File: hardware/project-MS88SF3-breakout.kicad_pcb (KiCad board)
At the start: 4 copper layers, 22.9 x 50.8 mm, 28 parts, among them J1 Conn_02x05_Odd_Even, J2 S2B-PH-SM4-TB(LF)(SN), J3 USB4105-GF-A, J4 Conn_01x12_Male, J5 Conn_01x16_Male, U1 MS88SF3_NRF52840

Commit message: Update pcb from schematic
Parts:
- removed Ref**: Val**, drawing:bear-body_silk_16x16
- removed S1: 435151014824, 435151014824:435151014824
- added SW1: PTS810_SJM_250_SMTR_LFS, PTS810-SJM-250-SMTR-LFS:SW_PTS810_SJM_250_SMTR_LFS, F.Cu at (25.3, 118.0)
- J4: value Conn_01x12_Male -> Conn_01x12_Pin; moved to F.Cu
- J5: value Conn_01x16_Male -> Conn_01x16_Pin; moved to F.Cu
- JP1: footprint Jumper:SolderJumper-2_P1.3mm_Bridged_RoundedPad1.0x1.5mm -> mine:SolderJumper-2_P1.3mm_Bridged_RoundedPad1.0x1.5mm
- JP2: footprint Jumper:SolderJumper-2_P1.3mm_Open_RoundedPad1.0x1.5mm -> mine:SolderJumper-2_P1.3mm_Open_RoundedPad1.0x1.5mm
- moved J5 38.6 mm to (19.1, 85.4), turned to 0 degrees
- moved J4 13.7 mm to (23.8, 85.4), turned to 0 degrees
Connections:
- J1 pad 7: Net-(J1-Pad7) -> unconnected-(J1-Pin_7-Pad7)
- J3 pad A8: Net-(J3-PadA8) -> unconnected-(J3-SBU1-PadA8)
- J3 pad B8: Net-(J3-PadB8) -> unconnected-(J3-SBU2-PadB8)
- J4 pad 11: Net-(J4-Pad11) -> unconnected-(J4-Pin_11-Pad11)
- J5 pad 4: /RX -> /P0.24
- J5 pad 6: /TX -> /P0.20
- U1 pad 11: Net-(U1-Pad11) -> unconnected-(U1-P0.28/AIN4-Pad11)
- U1 pad 12: Net-(U1-Pad12) -> unconnected-(U1-P0.30/AIN6-Pad12)
- U1 pad 13: Net-(U1-Pad13) -> unconnected-(U1-P0.31/AIN7-Pad13)
- U1 pad 14: Net-(U1-Pad14) -> unconnected-(U1-P0.27-Pad14)
- U1 pad 17: Net-(U1-Pad17) -> unconnected-(U1-P0.26-Pad17)
- U1 pad 19: Net-(U1-Pad19) -> /RX
- U1 pad 2: Net-(U1-Pad2) -> unconnected-(U1-P1.11-Pad2)
- U1 pad 20: Net-(U1-Pad20) -> /TX
- U1 pad 21: Net-(U1-Pad21) -> unconnected-(U1-P1.08-Pad21)
- U1 pad 22: Net-(U1-Pad22) -> unconnected-(U1-P0.11/TRACEDATA2-Pad22)
- U1 pad 23: Net-(U1-Pad23) -> unconnected-(U1-P0.00/XL1-Pad23)
- U1 pad 24: Net-(U1-Pad24) -> unconnected-(U1-P0.01/XL2-Pad24)
- U1 pad 25: Net-(U1-Pad25) -> unconnected-(U1-P0.08-Pad25)
- U1 pad 26: Net-(U1-Pad26) -> unconnected-(U1-P1.09/TRACEDATA3-Pad26)
- U1 pad 27: Net-(U1-Pad27) -> unconnected-(U1-P0.12/TRACEDATA1-Pad27)
- U1 pad 29: Net-(U1-Pad29) -> unconnected-(U1-P0.16-Pad29)
- U1 pad 3: Net-(U1-Pad3) -> unconnected-(U1-P1.12-Pad3)
- U1 pad 30: Net-(U1-Pad30) -> unconnected-(U1-P0.14-Pad30)
- U1 pad 44: /TX -> /P0.20
- U1 pad 46: /RX -> /P0.24
- U1 pad 47: Net-(U1-Pad47) -> unconnected-(U1-P1.00/TRACEDATA0-Pad47)
- U1 pad 51: Net-(U1-Pad51) -> unconnected-(U1-RF-Pad51)
- U1 pad 52: Net-(U1-Pad52) -> unconnected-(U1-P1.02-Pad52)
- U1 pad 53: Net-(U1-Pad53) -> unconnected-(U1-P1.04-Pad53)
- U1 pad 54: Net-(U1-Pad54) -> unconnected-(U1-P1.06-Pad54)
- U1 pad 57: Net-(U1-Pad57) -> unconnected-(U1-P1.07-Pad57)
- U1 pad 58: Net-(U1-Pad58) -> unconnected-(U1-P1.05-Pad58)
- U1 pad 59: Net-(U1-Pad59) -> unconnected-(U1-P1.01-Pad59)
- U1 pad 60: Net-(U1-Pad60) -> unconnected-(U1-P1.03-Pad60)
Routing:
- net /P0.20: track 0.00 -> 15.2 mm
- net /TX: track 34.6 -> 19.4 mm
- net /P0.24: track 0.00 -> 11.4 mm
- net /RX: track 37.1 -> 25.7 mm

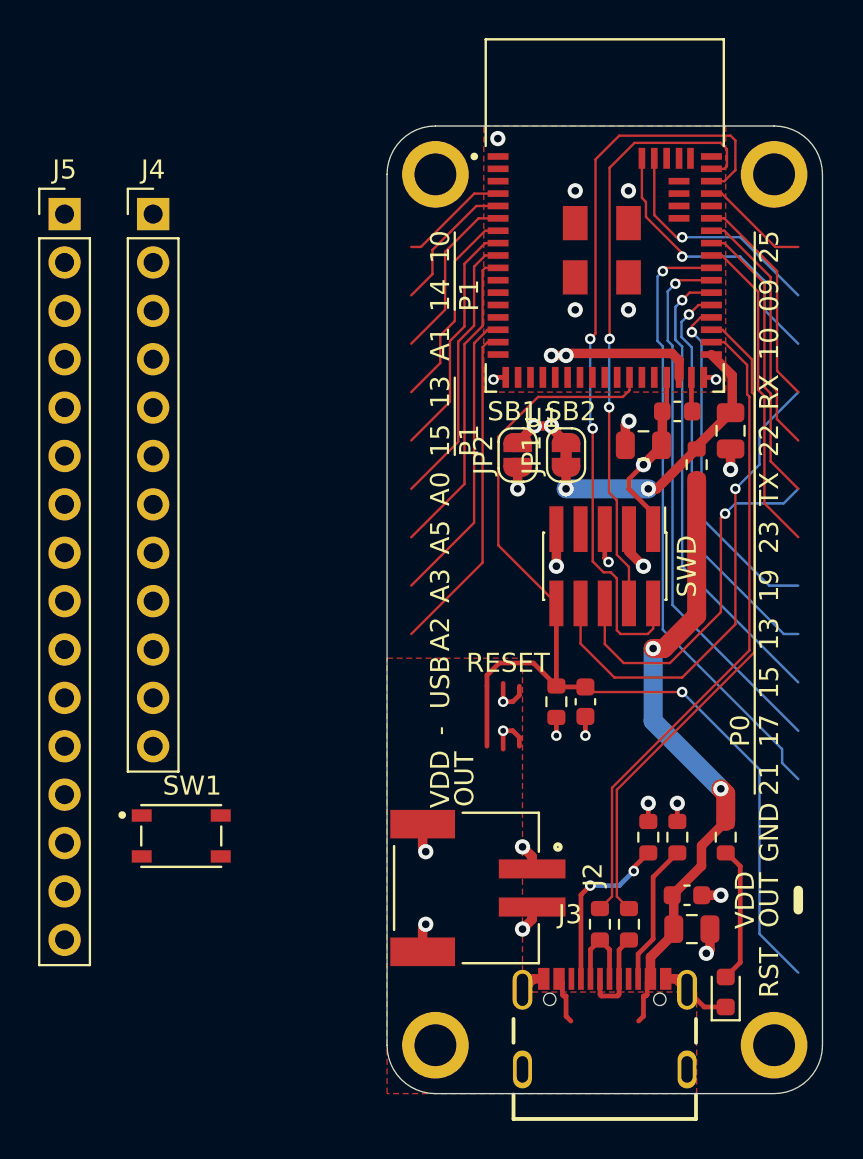
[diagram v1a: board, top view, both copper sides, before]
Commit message: Remove unused traces
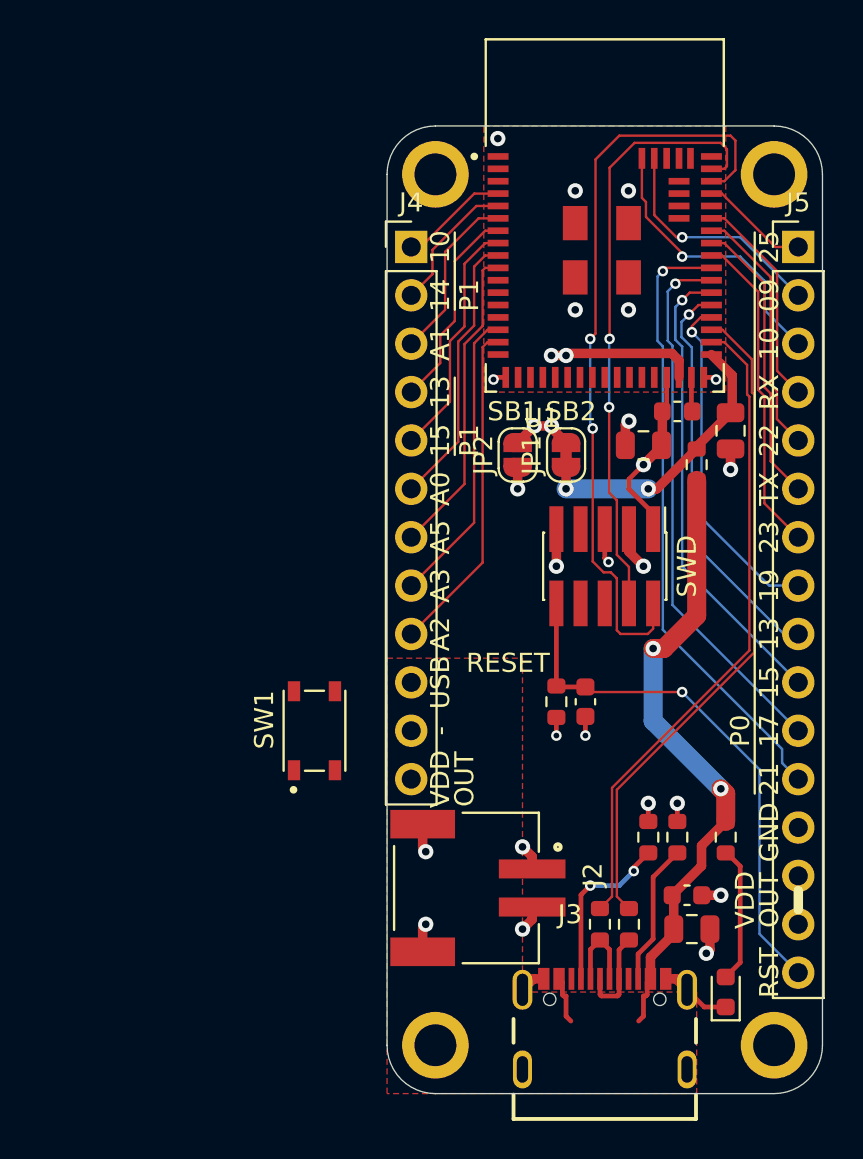
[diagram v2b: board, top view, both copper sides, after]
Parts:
- moved J5 38.6 mm to (57.7, 87.1)
- moved J4 13.7 mm to (37.3, 87.1)
- moved SW1 8.91 mm to (32.3, 112.5), turned to 90 degrees
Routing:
- net /RESET: track 55.1 -> 28.3 mm
- net /RX: track 25.7 -> 0.00 mm, vias 1 -> 0
- net /TX: track 19.4 -> 0.00 mm, vias 1 -> 0
- net GND: track 29.5 -> 24.6 mm, vias 22 -> 20

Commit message: Update pin headers from schematic
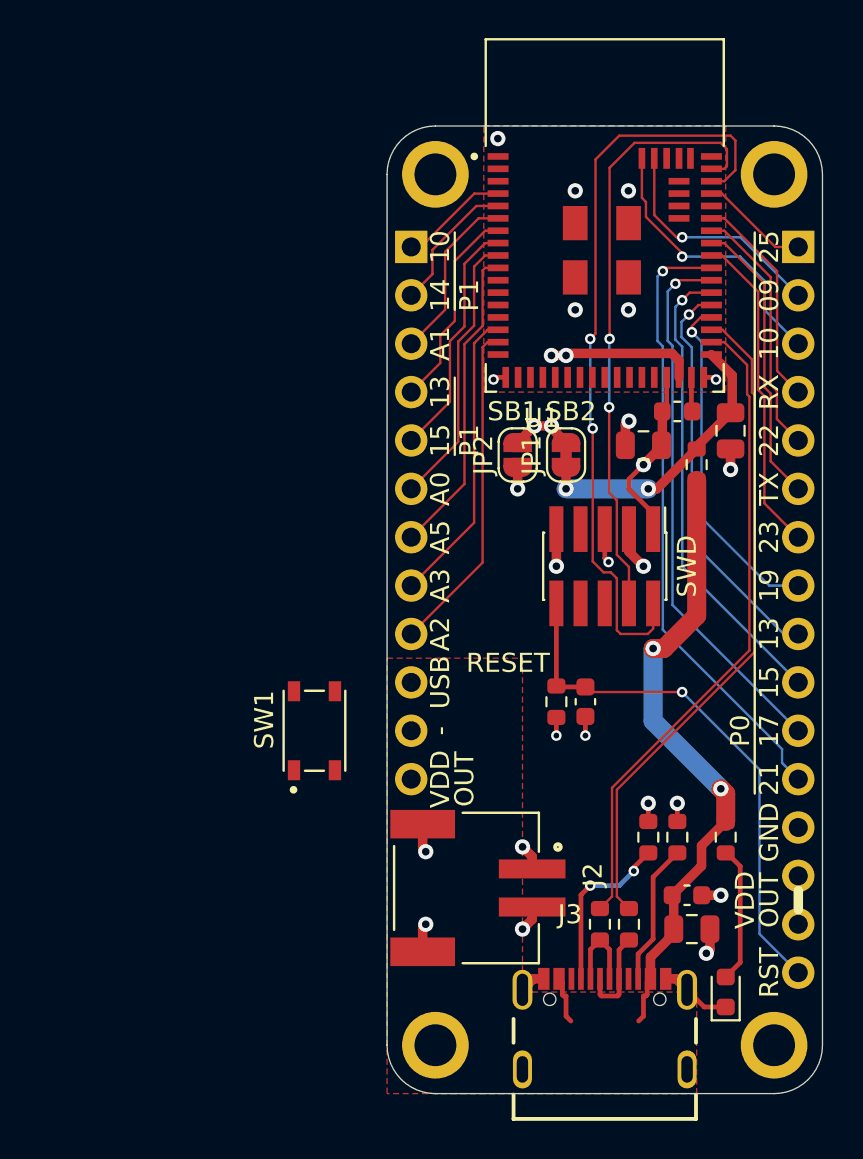
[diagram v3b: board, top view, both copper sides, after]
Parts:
- J4: footprint Connector_PinHeader_2.54mm:PinHeader_1x12_P2.54mm_Vertical -> mine:PinHeader_1x12_P2.54mm_Vertical
- J5: footprint Connector_PinHeader_2.54mm:PinHeader_1x16_P2.54mm_Vertical -> mine:PinHeader_1x16_P2.54mm_Vertical
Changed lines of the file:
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@@
 		)
 	)
-	(footprint "Connector_PinHeader_2.54mm:PinHeader_1x16_P2.54mm_Vertical"
+	(footprint "mine:PinHeader_1x16_P2.54mm_Vertical"
 		(layer "F.Cu")
 		(at 57.658 87.122)
@@
 		(property "Reference" "J5"
 			(at 0 -2.33 0)
-			(layer "F.SilkS")
+			(layer "F.Fab")
 			(effects
 				(font
@@
 			)
 		)
-		(property "Footprint" "Connector_PinHeader_2.54mm:PinHeader_1x16_P2.54mm_Vertical"
+		(property "Footprint" "mine:PinHeader_1x16_P2.54mm_Vertical"
 			(at 0 0 0)
 			(unlocked yes)
@@
 		(attr through_hole)
 		(fp_line
-			(start -1.33 -1.33)
-			(end 0 -1.33)
-			(stroke
-				(width 0.12)
-				(type solid)
-			)
-			(layer "F.SilkS")
-		)
-		(fp_line
-			(start -1.33 0)
-			(end -1.33 -1.33)
-			(stroke
-				(width 0.12)
-				(type solid)
-			)
-			(layer "F.SilkS")
-		)
-		(fp_line
-			(start -1.33 1.27)
-			(end -1.33 39.43)
-			(stroke
-				(width 0.12)
-				(type solid)
-			)
-			(layer "F.SilkS")
-		)
-		(fp_line
-			(start -1.33 1.27)
-			(end 1.33 1.27)
-			(stroke
-				(width 0.12)
-				(type solid)
-			)
-			(layer "F.SilkS")
-		)
-		(fp_line
-			(start -1.33 39.43)
-			(end 1.33 39.43)
-			(stroke
-				(width 0.12)
-				(type solid)
-			)
-			(layer "F.SilkS")
-		)
-		(fp_line
-			(start 1.33 1.27)
-			(end 1.33 39.43)
-			(stroke
-				(width 0.12)
-				(type solid)
-			)
-			(layer "F.SilkS")
-		)
-		(fp_line
 			(start -1.8 -1.8)
 			(end -1.8 39.9)
@@
 		)
 	)
-	(footprint "Connector_PinHeader_2.54mm:PinHeader_1x12_P2.54mm_Vertical"
+	(footprint "mine:PinHeader_1x12_P2.54mm_Vertical"
 		(layer "F.Cu")
 		(at 37.338 87.122)
@@
 		(property "Reference" "J4"
 			(at 0 -2.33 0)
-			(layer "F.SilkS")
+			(layer "F.Fab")
 			(effects
 				(font
@@
 			)
 		)
-		(property "Footprint" "Connector_PinHeader_2.54mm:PinHeader_1x12_P2.54mm_Vertical"
+		(property "Footprint" "mine:PinHeader_1x12_P2.54mm_Vertical"
 			(at 0 0 0)
 			(unlocked yes)
@@
 		(attr through_hole)
 		(fp_line
-			(start -1.33 -1.33)
-			(end 0 -1.33)
-			(stroke
-				(width 0.12)
-				(type solid)
-			)
-			(layer "F.SilkS")
-		)
-		(fp_line
-			(start -1.33 0)
-			(end -1.33 -1.33)
-			(stroke
-				(width 0.12)
-				(type solid)
-			)
-			(layer "F.SilkS")
-		)
-		(fp_line
-			(start -1.33 1.27)
-			(end -1.33 29.27)
-			(stroke
-				(width 0.12)
-				(type solid)
-			)
-			(layer "F.SilkS")
-		)
-		(fp_line
-			(start -1.33 1.27)
-			(end 1.33 1.27)
-			(stroke
-				(width 0.12)
-				(type solid)
-			)
-			(layer "F.SilkS")
-		)
-		(fp_line
-			(start -1.33 29.27)
-			(end 1.33 29.27)
-			(stroke
-				(width 0.12)
-				(type solid)
-			)
-			(layer "F.SilkS")
-		)
-		(fp_line
-			(start 1.33 1.27)
-			(end 1.33 29.27)
-			(stroke
-				(width 0.12)
-				(type solid)
-			)
-			(layer "F.SilkS")
-		)
-		(fp_line
 			(start -1.8 -1.8)

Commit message: Place new button
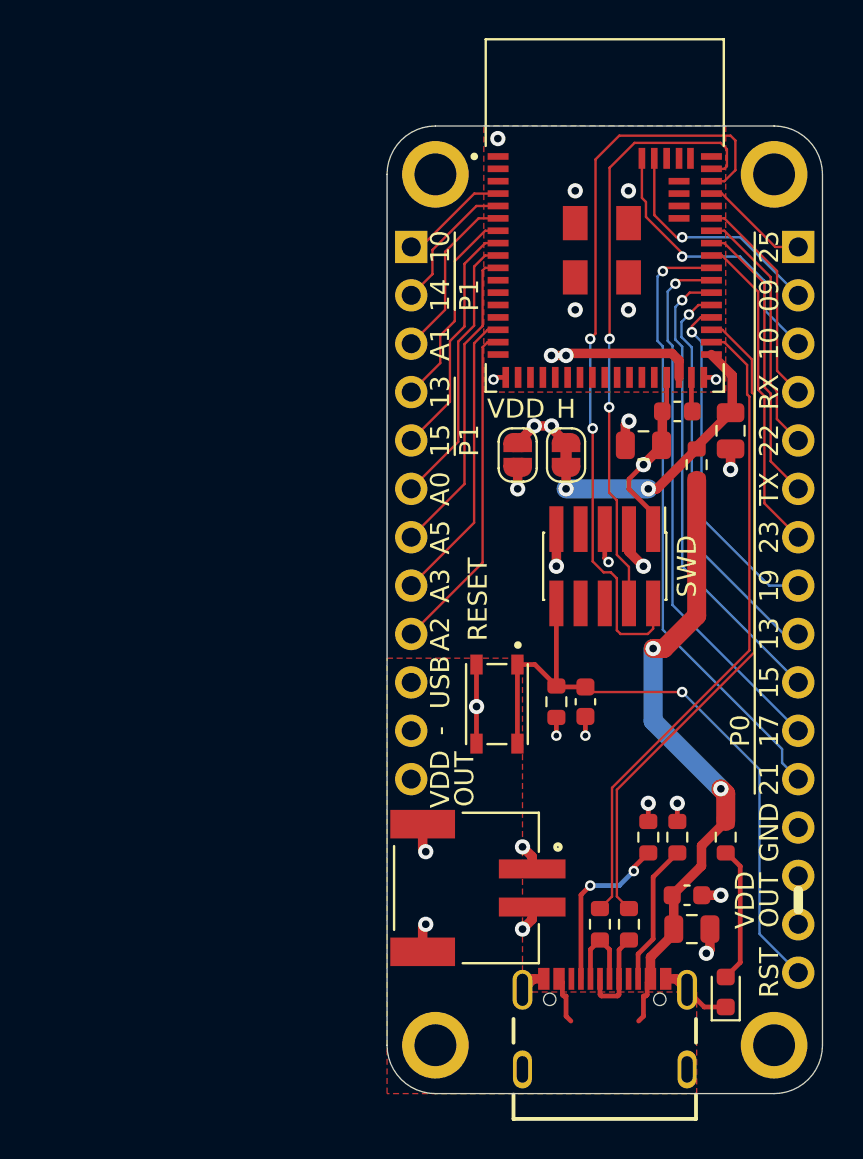
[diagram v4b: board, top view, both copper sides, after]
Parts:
- J4, J5: moved to B.Cu
- moved SW1 9.68 mm to (41.8, 111.1), turned to -90 degrees
- turned J4 to 180 degrees
- turned J5 to 180 degrees
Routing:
- net /RESET: track 28.3 -> 35.0 mm
- net GND: track 24.6 -> 28.8 mm, vias 20 -> 21
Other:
- board text added: "H"
- board text removed: "SB1"
- board text removed: "SB2"

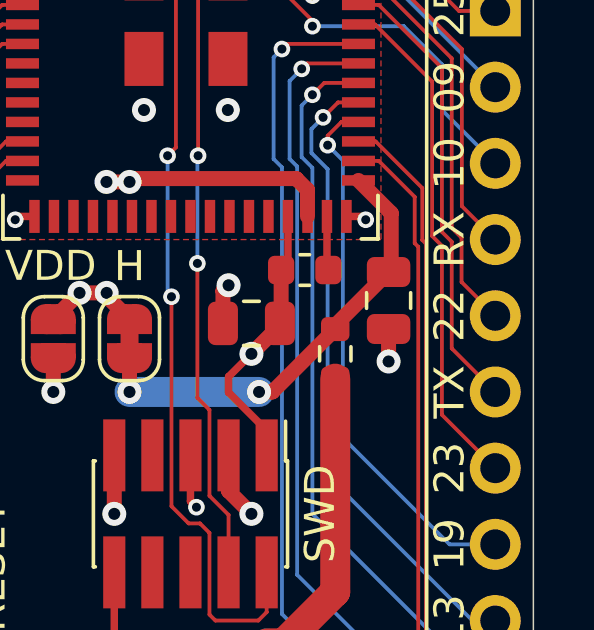
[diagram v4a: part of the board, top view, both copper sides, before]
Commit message: Change old RX/TX pin silkscreen
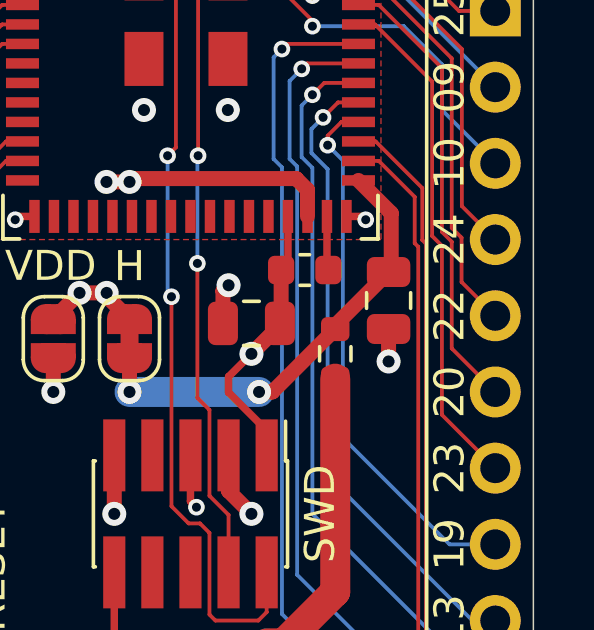
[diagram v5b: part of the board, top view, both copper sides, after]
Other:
- board text added: "20"
- board text added: "24"
- board text removed: "RX"
- board text removed: "TX"
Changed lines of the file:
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@@
 		)
 	)
-	(gr_text "RX"
+	(gr_text "24"
 		(at 56.134 94.742 90)
 		(layer "F.SilkS")
@@
 		)
 	)
-	(gr_text "TX"
+	(gr_text "20"
 		(at 56.134 99.822 90)
 		(layer "F.SilkS")

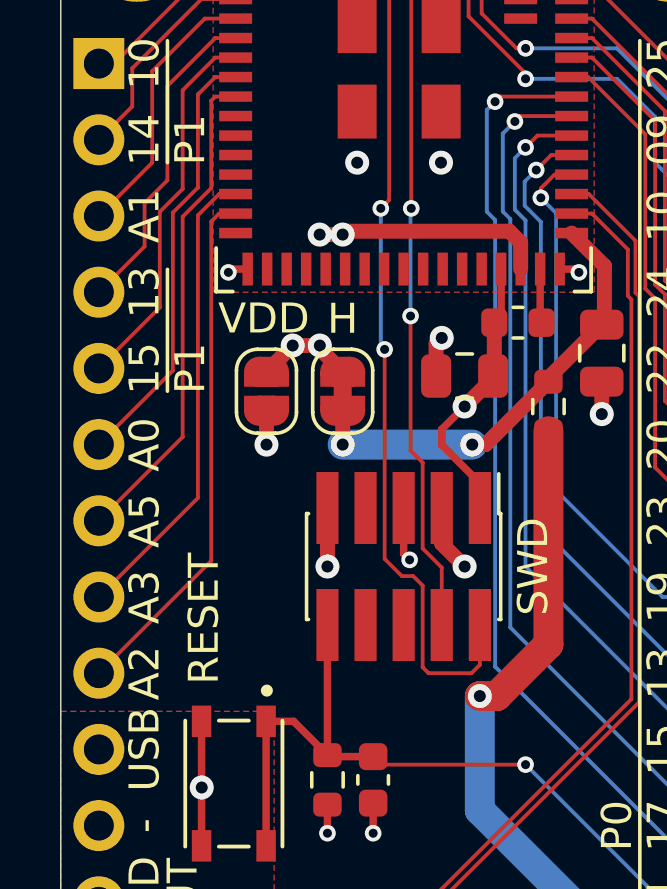
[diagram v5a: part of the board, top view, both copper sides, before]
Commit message: Send all alternate silkscreen to the back
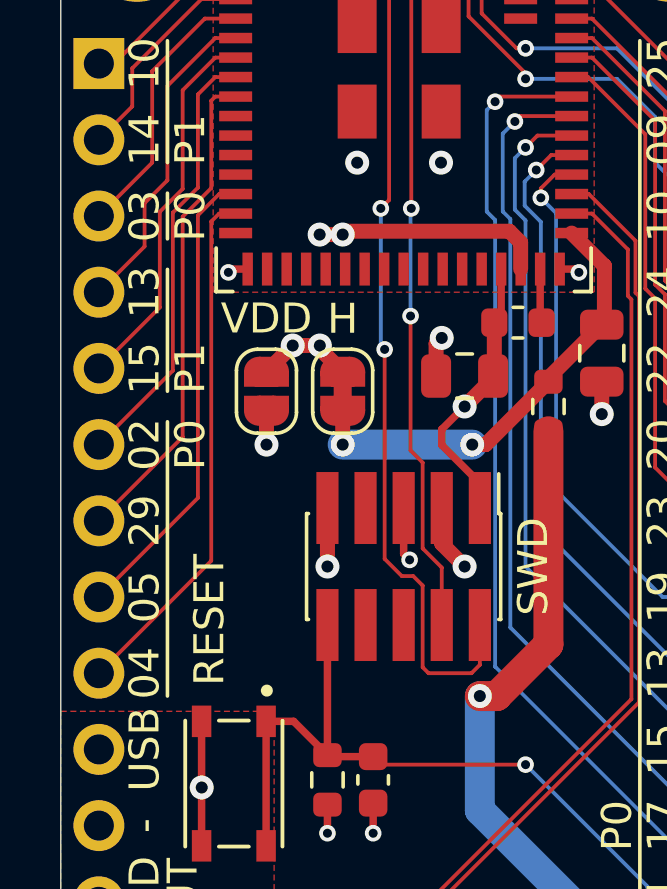
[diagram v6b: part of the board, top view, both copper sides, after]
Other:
- board text added: "02"
- board text added: "03"
- board text added: "04"
- board text added: "05"
- board text added: "29"
- board text removed: "P0.20"
- board text removed: "P0.24"
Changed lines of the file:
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@@
+	)
+	(gr_line
+		(start 39.624 92.964)
+		(end 39.624 91.44)
+		(stroke
+			(width 0.12)
+			(type solid)
+		)
+		(layer "F.SilkS")
+	)
+	(gr_line
+		(start 39.624 108.204)
+		(end 39.624 99.06)
+		(stroke
+			(width 0.12)
+			(type solid)
+		)
+		(layer "F.SilkS")
 	)
 	(gr_line
@@
 		(layer "Edge.Cuts")
 	)
-	(gr_text "P0.24"
-		(at 54.102 94.742 0)
+	(gr_text "A1"
+		(at 39.624 92.202 0)
+		(layer "B.SilkS")
+		(effects
+			(font
+				(size 1 1)
+				(thickness 0.15)
+			)
+			(justify mirror)
+		)
+	)
+	(gr_text "A2"
+		(at 39.624 107.442 0)
+		(layer "B.SilkS")
+		(effects
+			(font
+				(size 1 1)
+				(thickness 0.15)
+			)
+			(justify mirror)
+		)
+	)
+	(gr_text "A0"
+		(at 39.624 99.822 0)
+		(layer "B.SilkS")
+		(effects
+			(font
+				(size 1 1)
+				(thickness 0.15)
+			)
+			(justify mirror)
+		)
+	)
+	(gr_text "A3"
+		(at 39.624 104.902 0)
 		(layer "B.SilkS")
 		(effects
@@
 		)
 	)
+	(gr_text "A5"
+		(at 39.624 102.362 0)
+		(layer "B.SilkS")
+		(effects
+			(font
+				(size 1 1)
+				(thickness 0.15)
+			)
+			(justify mirror)
+		)
+	)
 	(gr_text "François Gervais\n27 août 2022\nv"
 		(at 54.356 83.82 0)
@@
 		)
 	)
-	(gr_text "P0.20"
-		(at 54.102 99.822 0)
-		(layer "B.SilkS")
-		(effects
-			(font
-				(size 1 1)
-				(thickness 0.15)
-			)
-			(justify mirror)
-		)
-	)
 	(gr_text "GND"
 		(at 56.134 117.856 90)
@@
 	)
 	(gr_text "RESET"
-		(at 40.838 105.622 90)
+		(at 41.021 105.664 90)
 		(layer "F.SilkS" knockout)
 		(effects
@@
 	)
 	(gr_text "VDD"
-		(at 42.838 95.622 0)
+		(at 42.926 95.622 0)
 		(layer "F.SilkS")
 		(effects
@@
 		)
 	)
-	(gr_text "A1"
-		(at 38.862 92.202 90)
+	(gr_text "29"
+		(at 38.862 102.362 90)
 		(layer "F.SilkS")
 		(effects
@@
 		)
 	)
-	(gr_text "A2"
+	(gr_text "05"
+		(at 38.862 104.902 90)
+		(layer "F.SilkS")
+		(effects
+			(font
+				(size 1 1)
+				(thickness 0.15)
+			)
+		)
+	)
+	(gr_text "04"
 		(at 38.862 107.442 90)
-		(layer "F.SilkS")
-		(effects
-			(font
-				(size 1 1)
-				(thickness 0.15)
-			)
-		)
-	)
-	(gr_text "A0"
-		(at 38.862 99.822 90)
-		(layer "F.SilkS")
-		(effects
-			(font
-				(size 1 1)
-				(thickness 0.15)
-			)
-		)
-	)
-	(gr_text "A3"
-		(at 38.862 104.902 90)
 		(layer "F.SilkS")
 		(effects
@@
 		)
 	)
-	(gr_text "A5"
-		(at 38.862 102.362 90)
-		(layer "F.SilkS")
-		(effects
-			(font
-				(size 1 1)
-				(thickness 0.15)
-			)
-		)
-	)
 	(gr_text "15"
 		(at 38.862 97.282 90)
@@
 		)
 	)
+	(gr_text "02"
+		(at 38.862 99.822 90)
+		(layer "F.SilkS")
+		(effects
+			(font
+				(size 1 1)
+				(thickness 0.15)
+			)
+		)
+	)
 	(gr_text "H"
 		(at 45.466 95.631 0)
@@
 		)
 	)
+	(gr_text "P0"
+		(at 40.386 99.822 90)
+		(layer "F.SilkS")
+		(effects
+			(font
+				(size 1 1)
+				(thickness 0.15)
+			)
+		)
+	)
 	(gr_text "19"
 		(at 56.134 104.902 90)
 		(layer "F.SilkS")
 		(effects
+			(font
+				(size 1 1)
+				(thickness 0.15)
+			)
+		)
+	)
+	(gr_text "P0"
+		(at 40.386 92.202 90)
+		(layer "F.SilkS")
+		(effects
+			(font
+				(size 1 1)
+				(thickness 0.15)
+			)
+		)
+	)
+	(gr_text "03"
+		(at 38.862 92.202 90)
+		(layer "F.SilkS")
+		(effects
